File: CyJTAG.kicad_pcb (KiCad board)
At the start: 2 copper layers, 29.8 x 22.9 mm, 12 parts, among them P1 USB_B, P2 CONN_02X04, P3 CONN_02X04, P4 CONN_02X06, SW1 Switch_SPDT, U1 CY7C65215, U2 TLV70233DBV

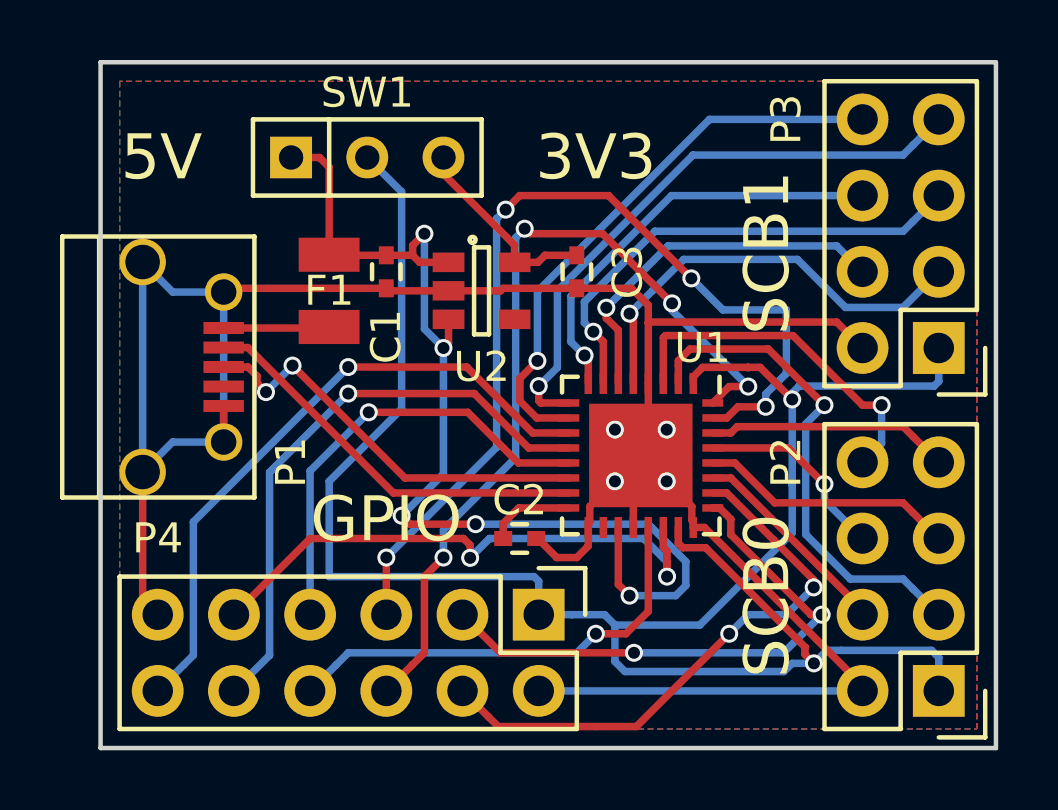
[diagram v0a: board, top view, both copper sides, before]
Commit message: Simplified board by removing GPIO header and adding power, Rx, and Tx LEDs
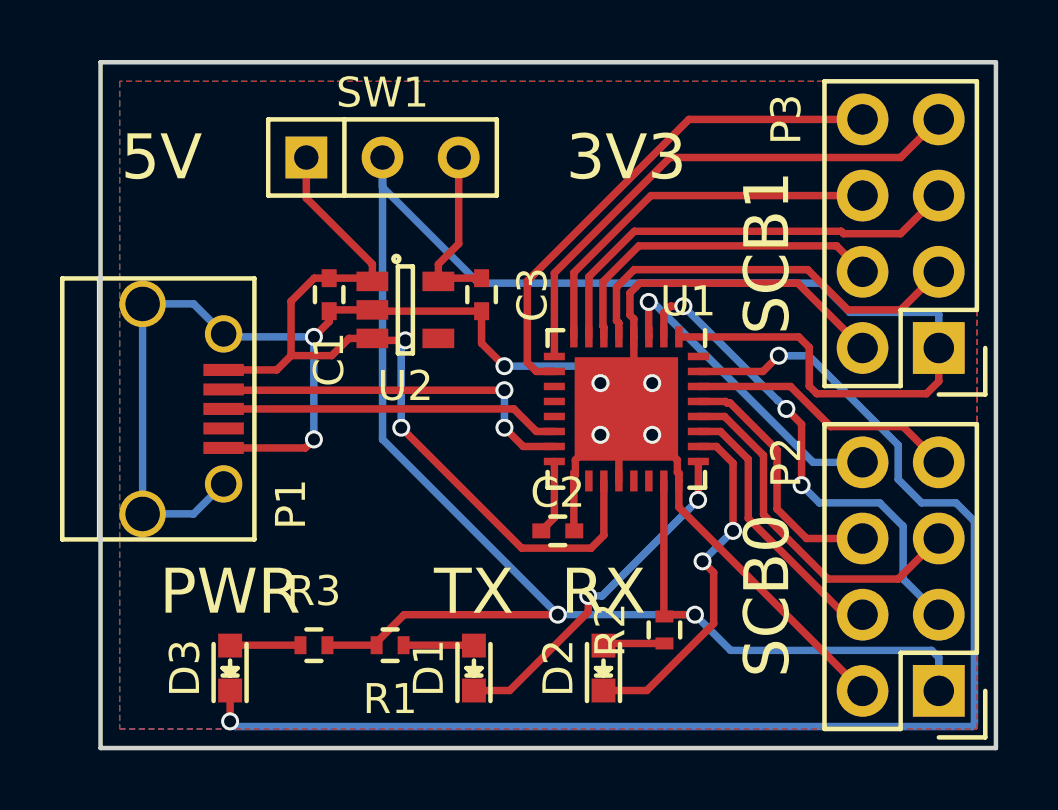
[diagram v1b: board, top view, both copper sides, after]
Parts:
- removed ?: Symbol_OSHW-Logo_SilkScreen, Symbols:Symbol_OSHW-Logo_SilkScreen
- removed F1: FUSE, Fuse_Holders_and_Fuses:Fuse_SMD1206_Reflow
- removed P4: CONN_02X06, Pin_Headers:Pin_Header_Straight_2x06
- added D1: LED, LEDs:LED-0603, F.Cu at (110.2, 114.8)
- added D2: LED, LEDs:LED-0603, F.Cu at (114.6, 114.8)
- added D3: LED, LEDs:LED-0603, F.Cu at (102.1, 114.8)
- added R1: 1k, Resistors_SMD:R_0402, F.Cu at (107.4, 114.0)
- added R2: 1k, Resistors_SMD:R_0402, F.Cu at (116.6, 113.5)
- added R3: 1k, Resistors_SMD:R_0402, F.Cu at (104.9, 114.0)
- moved C3 3.27 mm to (110.5, 102.4)
- moved U2 2.62 mm to (108.0, 102.9)
- moved C1 2.05 mm to (105.4, 102.4)
- moved U1 1.62 mm to (115.3, 106.2)
- moved P1 1.40 mm to (100.3, 106.2)
- moved C2 1.30 mm to (113.0, 110.2)
- moved SW1 0.51 mm to (107.2, 97.8)
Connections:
- P1 pad 1: Net-(F1-Pad1) -> +5V
- P1 pad 2: /USBDP -> /USBDM
- P1 pad 3: /USBDM -> /USBDP
- U1 pad 11: /SUSPEND -> (no net)
- U1 pad 12: /WAKEUP -> (no net)
- U1 pad 13: /GPIO_16 -> (no net)
- U1 pad 14: /USBDM -> /USBDP
- U1 pad 15: /USBDP -> /USBDM
- U1 pad 21: /GPIO_17 -> (no net)
- U1 pad 22: /GPIO_18 -> (no net)
- U1 pad 25: /GPIO_0 -> //TXLED
- U1 pad 26: /GPIO_1 -> //RXLED
- U1 pad 31: /GPIO_6 -> //POWER
- U1 pad 32: /GPIO_7 -> (no net)
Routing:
- net //POWER: track 0.00 -> 45.1 mm, vias 0 -> 2
- net /GPIO_6: track 31.7 -> 0.00 mm, vias 4 -> 0
- net /GPIO_7: track 28.5 -> 0.00 mm, vias 4 -> 0
- net /SUSPEND: track 21.7 -> 0.00 mm, vias 1 -> 0
- net /WAKEUP: track 19.6 -> 0.00 mm, vias 1 -> 0
- net /GPIO_1: track 18.9 -> 0.00 mm, vias 2 -> 0
- net /GPIO_18: track 18.8 -> 0.00 mm, vias 2 -> 0
- net /GPIO_0: track 18.5 -> 0.00 mm, vias 2 -> 0
- net /GPIO_17: track 15.2 -> 0.00 mm, vias 1 -> 0
- net /GPIO_16: track 14.9 -> 0.00 mm, vias 1 -> 0
- net GND: track 84.9 -> 70.4 mm, vias 4 -> 7
- net //RXLED: track 0.00 -> 11.9 mm, vias 0 -> 2
- net //TXLED: track 0.00 -> 11.7 mm, vias 0 -> 2
- net VDD: track 68.9 -> 79.7 mm
- net +5V: track 35.9 -> 29.8 mm, vias 5 -> 2
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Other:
- rule via_min_drill: 0.3 -> 0.3302
- rule via_min_size: 0.381 -> 0.508
- board text added: "PWR"
- board text added: "RX"
- board text added: "TX"
- board text removed: "GPIO"

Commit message: Changed license to CERN OHL v1.2
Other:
- board text added: "CERN OHL v1.2"
- board text removed: "CC-BY-SA 4.0"
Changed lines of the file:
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@@
     (effects (font (size 1.5 1.5) (thickness 0.3)) (justify left mirror))
   )
-  (gr_text "CC-BY-SA 4.0" (at 120.65 104.394) (layer B.SilkS)
+  (gr_text "CERN OHL v1.2" (at 120.65 104.394) (layer B.SilkS)
     (effects (font (size 0.8 0.8) (thickness 0.15)) (justify left mirror))
   )
